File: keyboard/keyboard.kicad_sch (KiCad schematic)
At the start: 144 parts, among them J1 USB_C_Receptacle, J4 ISP, SW1 RESET, U1 ATmega32U4-A, Y1 16MHz

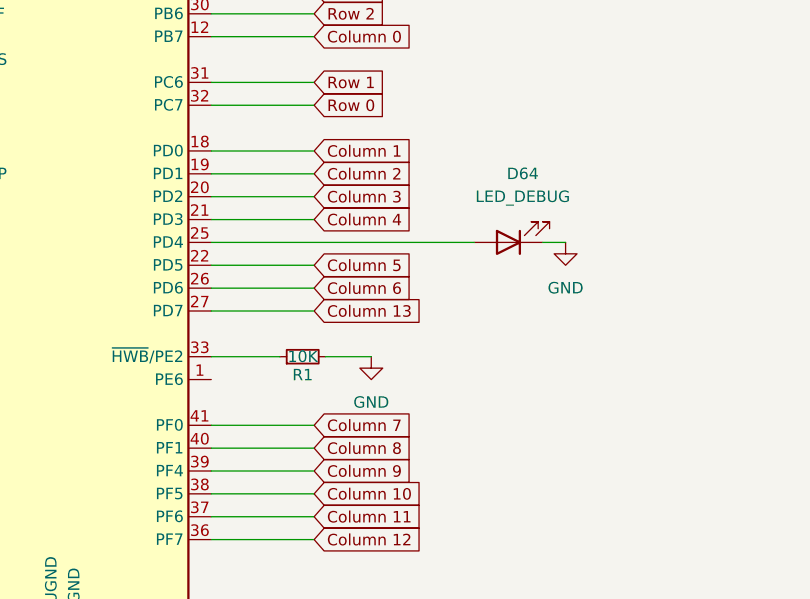
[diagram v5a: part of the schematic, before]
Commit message: Updated PCB layout, added caps
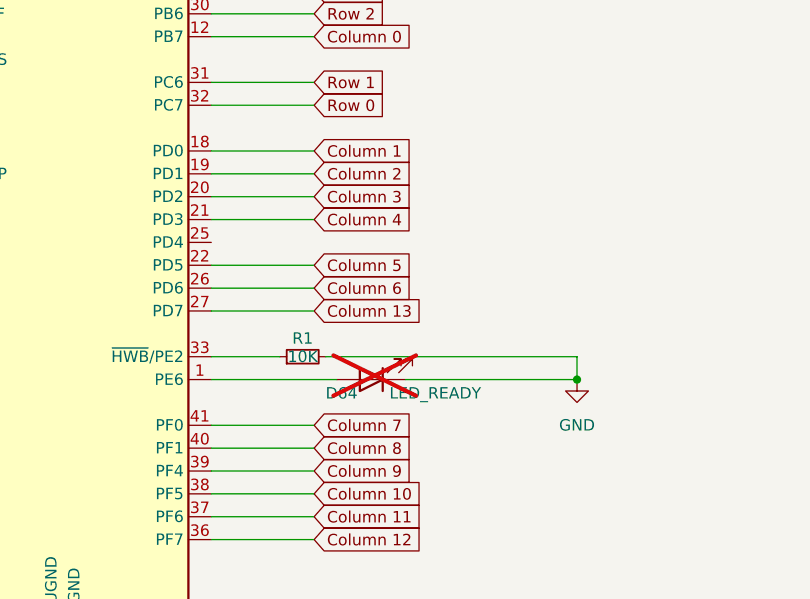
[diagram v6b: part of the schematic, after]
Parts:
- D64: value LED_DEBUG -> LED_READY; now not fitted
- S14: footprint sandpiperfootprints:SW_Cherry_MX_1.00u_PCB -> Button_Switch_Keyboard:SW_Cherry_MX_2.00u_PCB
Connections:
- net at D64.2 (A): now also U1.1 (PE6); no longer U1.25 (PD4)
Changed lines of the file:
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@@
 	)
 	(junction
+		(at 256.54 224.79)
+		(diameter 0)
+		(color 0 0 0 0)
+	)
+	(junction
 		(at 166.37 233.68)
 		(diameter 0)
@@
 	(wire
 		(pts
-			(xy 228.6 222.25) (xy 233.68 222.25)
+			(xy 228.6 222.25) (xy 256.54 222.25)
 		)
 		(stroke
@@
 	(wire
 		(pts
+			(xy 215.9 224.79) (xy 229.87 224.79)
+		)
+		(stroke
+			(width 0)
+			(type default)
+		)
+	)
+	(wire
+		(pts
 			(xy 227.33 184.15) (xy 215.9 184.15)
 		)
@@
 	(wire
 		(pts
+			(xy 256.54 222.25) (xy 256.54 224.79)
+		)
+		(stroke
+			(width 0)
+			(type default)
+		)
+	)
+	(wire
+		(pts
 			(xy 185.42 156.21) (xy 185.42 158.75)
 		)
@@
 	(wire
 		(pts
-			(xy 215.9 209.55) (xy 245.11 209.55)
-		)
-		(stroke
-			(width 0)
-			(type default)
-		)
-	)
-	(wire
-		(pts
 			(xy 227.33 214.63) (xy 215.9 214.63)
 		)
@@
 	(wire
 		(pts
-			(xy 252.73 209.55) (xy 255.27 209.55)
+			(xy 237.49 224.79) (xy 256.54 224.79)
 		)
 		(stroke
@@
 	(symbol
 		(lib_id "power:GND")
-		(at 255.27 209.55 0)
+		(at 256.54 224.79 0)
 		(unit 1)
 		(exclude_from_sim no)
@@
 		(fields_autoplaced yes)
 		(property "Reference" "#PWR012"
-			(at 255.27 215.9 0)
+			(at 256.54 231.14 0)
 			(effects
 				(font
@@
 		)
 		(property "Value" "GND"
-			(at 255.27 214.63 0)
+			(at 256.54 229.87 0)
 			(effects
 				(font
@@
 		)
 		(property "Footprint" ""
-			(at 255.27 209.55 0)
+			(at 256.54 224.79 0)
 			(effects
 				(font
@@
 		)
 		(property "Datasheet" ""
-			(at 255.27 209.55 0)
+			(at 256.54 224.79 0)
 			(effects
 				(font
@@
 		)
 		(property "Description" "Power symbol creates a global label with name \"GND\" , ground"
-			(at 255.27 209.55 0)
+			(at 256.54 224.79 0)
 			(effects
 				(font
@@
 	)
 	(symbol
-		(lib_id "power:GND")
-		(at 233.68 222.25 0)
-		(unit 1)
-		(exclude_from_sim no)
-		(in_bom yes)
-		(on_board yes)
-		(dnp no)
-		(fields_autoplaced yes)
-		(property "Reference" "#PWR03"
-			(at 233.68 228.6 0)
-			(effects
-				(font
-					(size 1.27 1.27)
-				)
-				(hide yes)
-			)
-		)
-		(property "Value" "GND"
-			(at 233.68 227.33 0)
-			(effects
-				(font
-					(size 1.27 1.27)
-				)
-			)
-		)
-		(property "Footprint" ""
-			(at 233.68 222.25 0)
-			(effects
-				(font
-					(size 1.27 1.27)
-				)
-				(hide yes)
-			)
-		)
-		(property "Datasheet" ""
-			(at 233.68 222.25 0)
-			(effects
-				(font
-					(size 1.27 1.27)
-				)
-				(hide yes)
-			)
-		)
-		(property "Description" "Power symbol creates a global label with name \"GND\" , ground"
-			(at 233.68 222.25 0)
-			(effects
-				(font
-					(size 1.27 1.27)
-				)
-				(hide yes)
-			)
-		)
-		(pin "1"
-		)
-		(instances
-			(project "keyboard"
-				(path "/7d6c198a-735f-4c93-baa2-078ce01909c3"
-					(reference "#PWR03")
-					(unit 1)
-				)
-			)
-		)
-	)
-	(symbol
 		(lib_id "ScottoKeebs:Placeholder_Keyswitch")
 		(at 201.93 49.53 0)
@@
 			)
 		)
-		(property "Footprint" "sandpiperfootprints:SW_Cherry_MX_1.00u_PCB"
+		(property "Footprint" "Button_Switch_Keyboard:SW_Cherry_MX_2.00u_PCB"
 			(at 213.36 49.53 0)
 			(effects
@@
 	(symbol
 		(lib_id "Device:LED")
-		(at 248.92 209.55 180)
+		(at 233.68 224.79 180)
 		(unit 1)
 		(exclude_from_sim no)
 		(in_bom yes)
 		(on_board yes)
-		(dnp no)
-		(fields_autoplaced yes)
+		(dnp yes)
 		(property "Reference" "D64"
-			(at 250.5075 201.93 0)
+			(at 230.378 226.314 0)
 			(effects
 				(font
@@
 			)
 		)
-		(property "Value" "LED_DEBUG"
-			(at 250.5075 204.47 0)
+		(property "Value" "LED_READY"
+			(at 240.792 226.314 0)
 			(effects
 				(font
@@
 		)
 		(property "Footprint" "LED_SMD:LED_1206_3216Metric"
-			(at 248.92 209.55 0)
+			(at 233.68 224.79 0)
 			(effects
 				(font
@@
 		)
 		(property "Datasheet" "~"
-			(at 248.92 209.55 0)
+			(at 233.68 224.79 0)
 			(effects
 				(font
@@
 		)
 		(property "Description" "Light emitting diode"
-			(at 248.92 209.55 0)
+			(at 233.68 224.79 0)
 			(effects
 				(font
@@
 		(dnp no)
 		(property "Reference" "R1"
-			(at 226.06 224.282 90)
+			(at 226.06 220.218 90)
 			(effects
 				(font
